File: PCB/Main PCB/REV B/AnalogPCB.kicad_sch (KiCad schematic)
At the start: 77 parts, among them J1 DF12NB_4.0_-20DP-0.5V_51_, J2 393570002, J3 393570002, J4 393570002, J5 393570002, J6 SJ3-35053D, Q1 2N7002, Q2 2N7002, Q3 2N7002, U1 ALDP105W, U2 ALDP105W, U3 ALDP105W

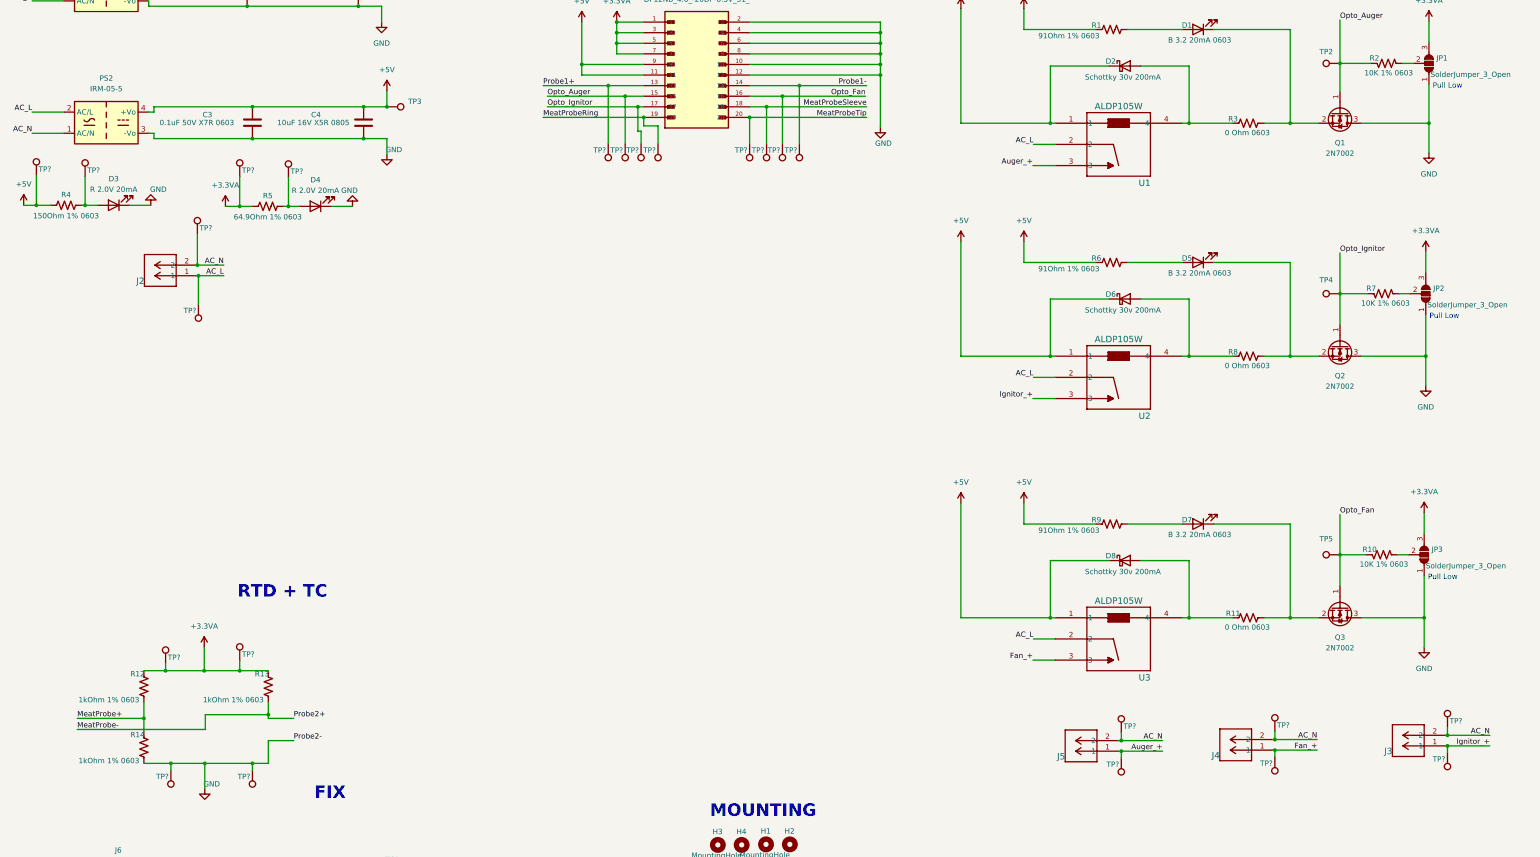
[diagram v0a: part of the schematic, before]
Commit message: PCB - Grouping for digital layout
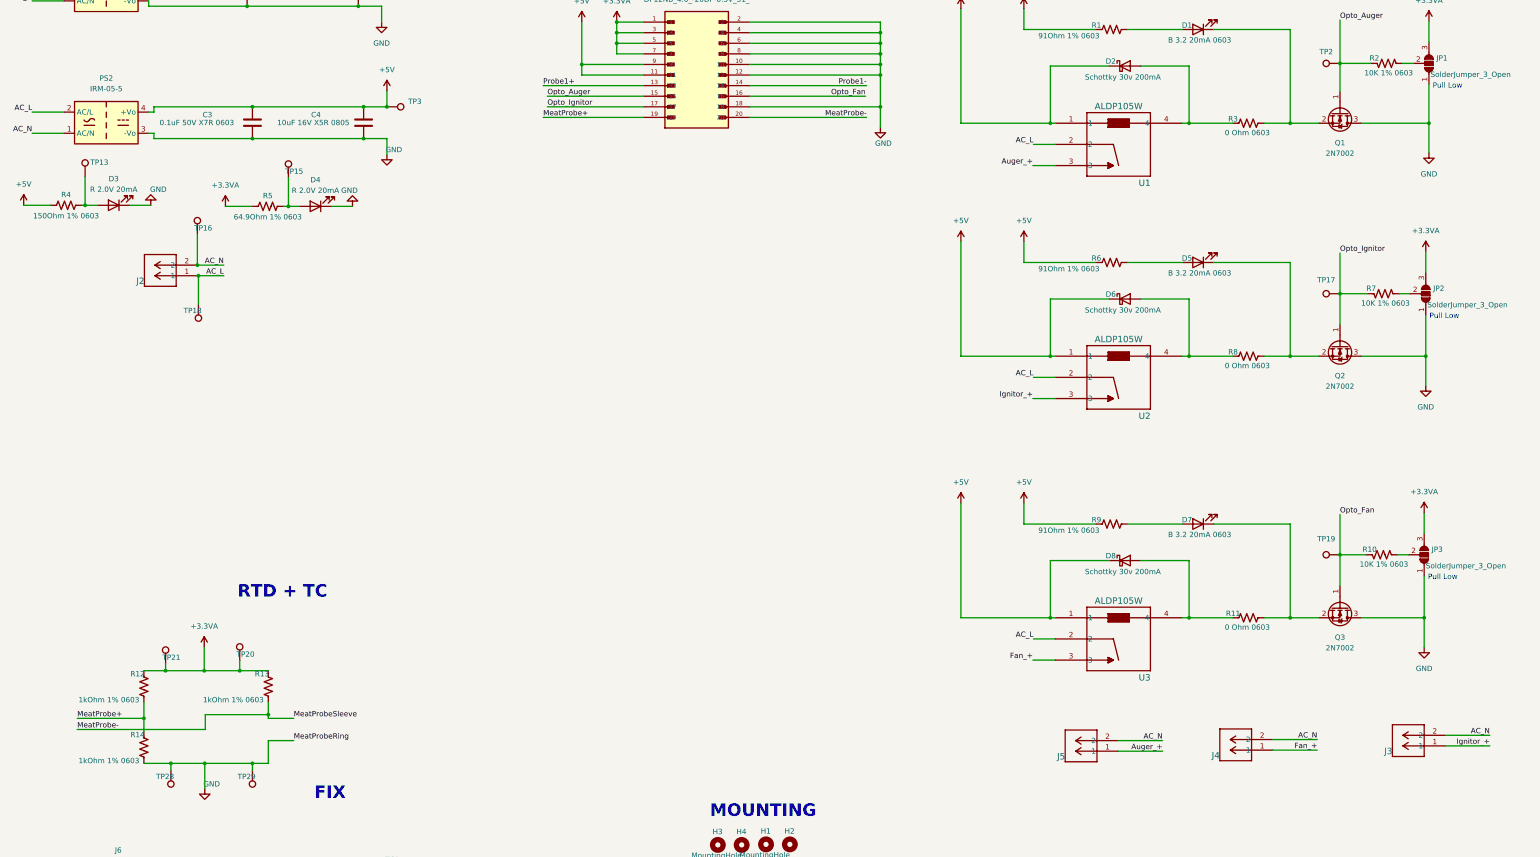
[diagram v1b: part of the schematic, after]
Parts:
- removed TP? (x16): TP, TestPoint:TestPoint_Pad_D1.0mm, symbol Connector:TestPoint
- gave numbers to parts that had none: 8
- renumbered TP4 to TP17, TP5 to TP19
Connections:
- net GND: now also J1.18, J6.3
- net MeatProbe+: now also J1.19
- net MeatProbe-: now also J1.20, J6.1
- net MeatProbeTip: no longer J1.20
- removed net MeatProbeRing: J1.19, J6.3
- removed net MeatProbeSleeve: J1.18, J6.1

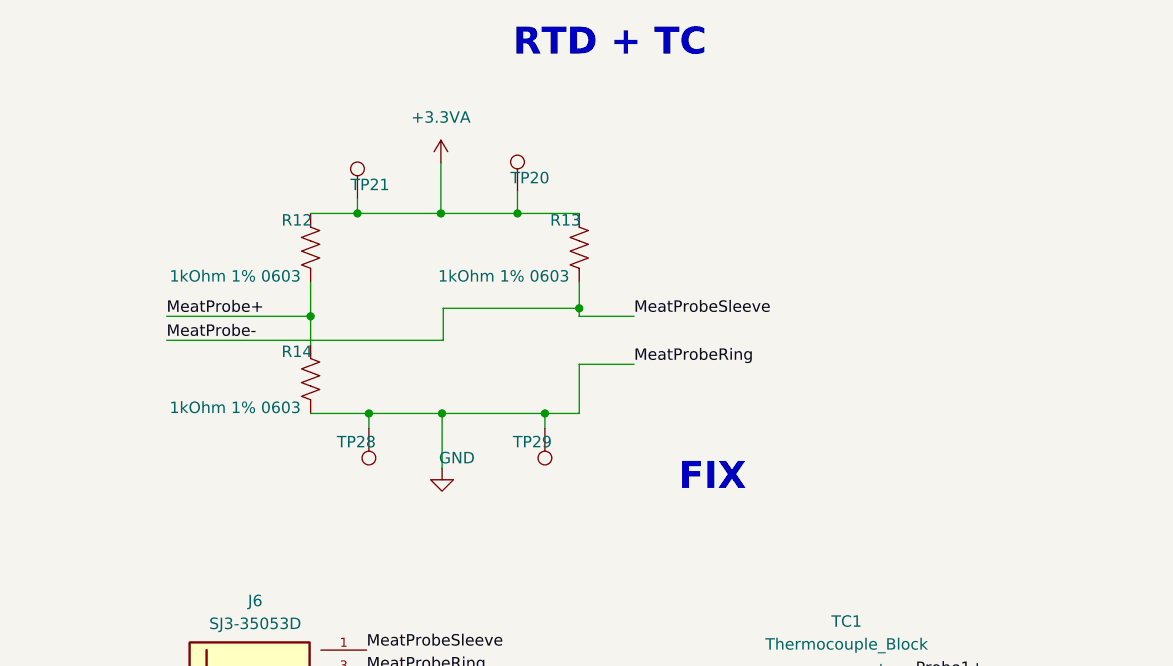
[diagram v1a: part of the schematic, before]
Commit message: PCB - Digital/analog layout complete - ready to review
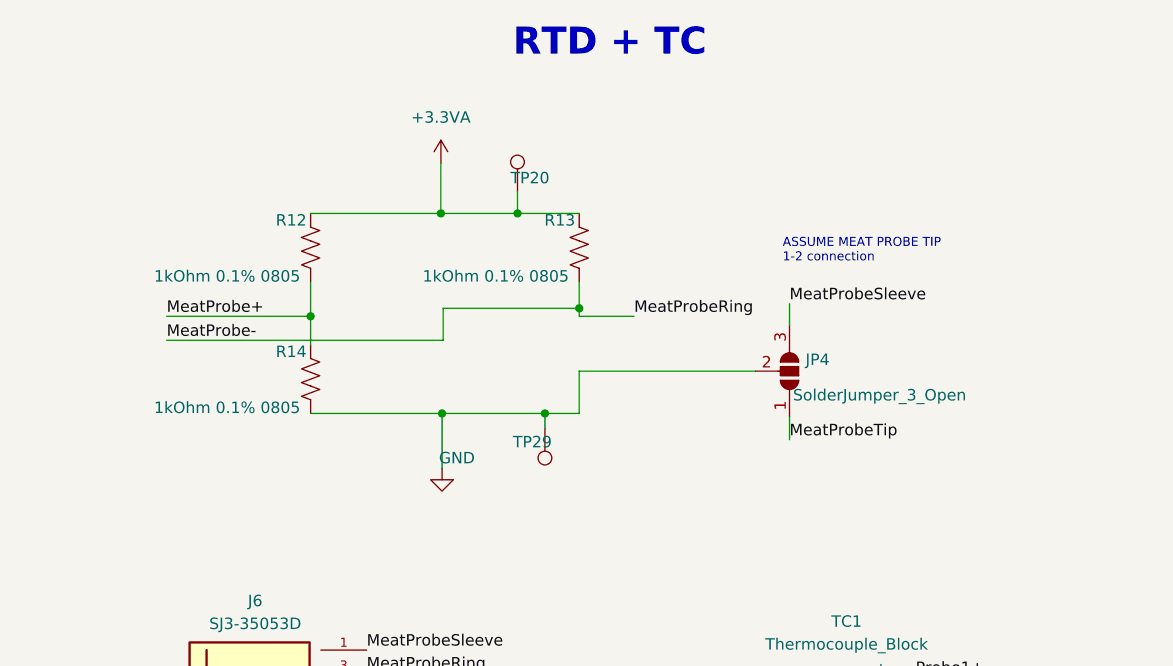
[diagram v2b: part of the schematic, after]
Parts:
- removed TP21, TP28: TP, TestPoint:TestPoint_Pad_D1.0mm, symbol Connector:TestPoint
- added JP4: SolderJumper_3_Open, Jumper:SolderJumper-3_P1.3mm_Open_RoundedPad1.0x1.5mm, symbol Jumper:SolderJumper_3_Open
- R12, R13, R14: value 1kOhm 1% 0603 -> 1kOhm 0.1% 0805; footprint Resistor_SMD:R_0603_1608Metric -> Resistor_SMD:R_0805_2012Metric; Manufacturer YAGEO -> Susumu; Manufacturer Part Number RC0603FR-071KL -> RG2012P-102-B-T5; Vendor Part Number 311-1.00KHRCT-ND -> RG20P1.0KBCT-ND
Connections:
- net GND: now also JP4.2 (C); no longer J6.3
- net MeatProbe-: now also J6.3; no longer J6.1
- net MeatProbeTip: now also JP4.1 (A)
- new net MeatProbeSleeve: J6.1, JP4.3 (B)
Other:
- note added: "ASSUME MEAT PROBE TIP 1-2 connection"
- note removed: "FIX"

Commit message: PCB - Analog pcb under review and making minor mods - diode placement
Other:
- note added: "Needs to have AC power to switch a load"
- moved on the sheet: C1, C2, C3, C4, D3, D4, H1, H2, H3, H4, J1, J2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

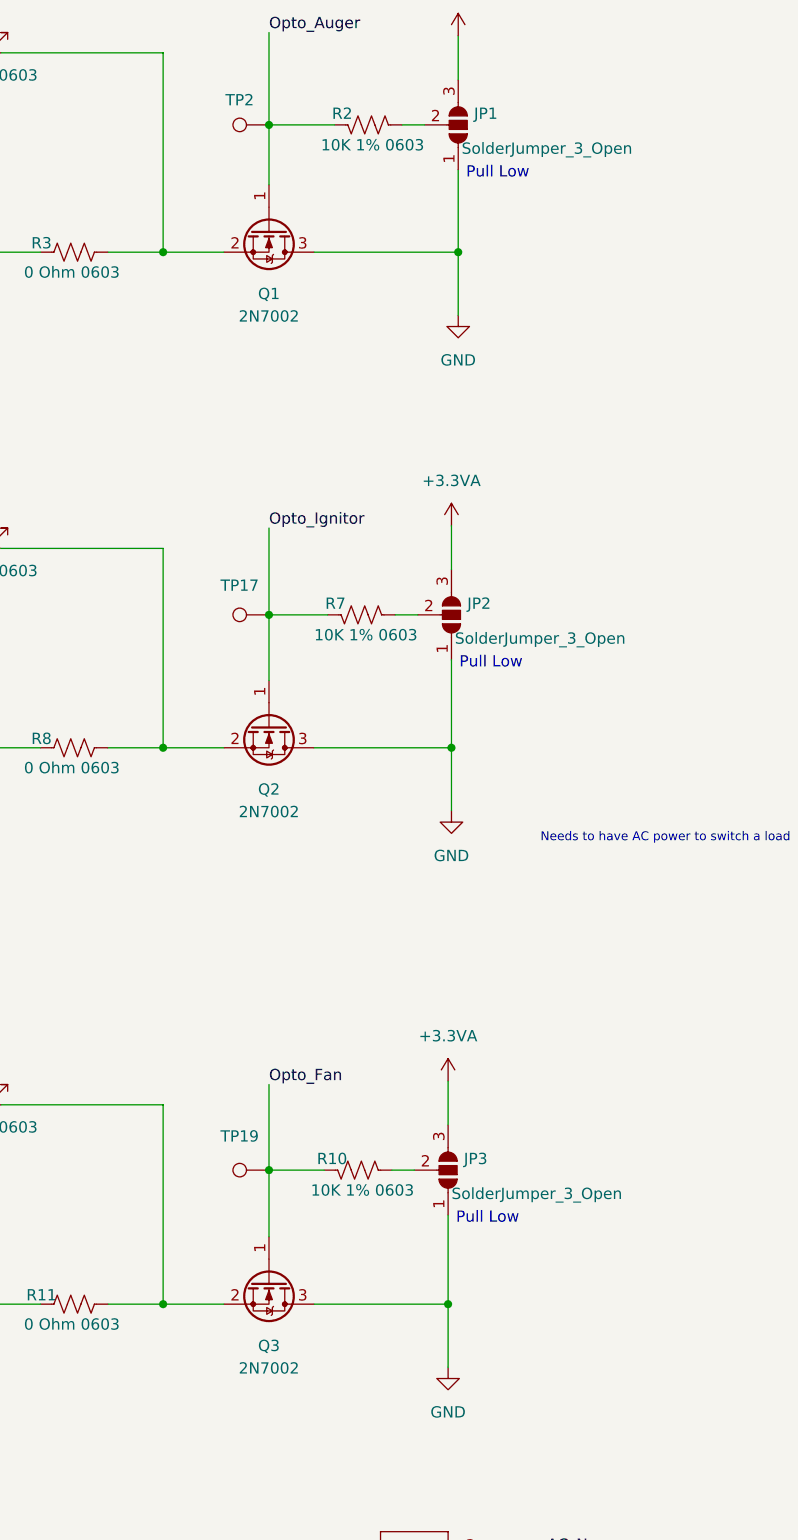
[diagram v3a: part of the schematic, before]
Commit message: PCB - gerbers generated and boms started
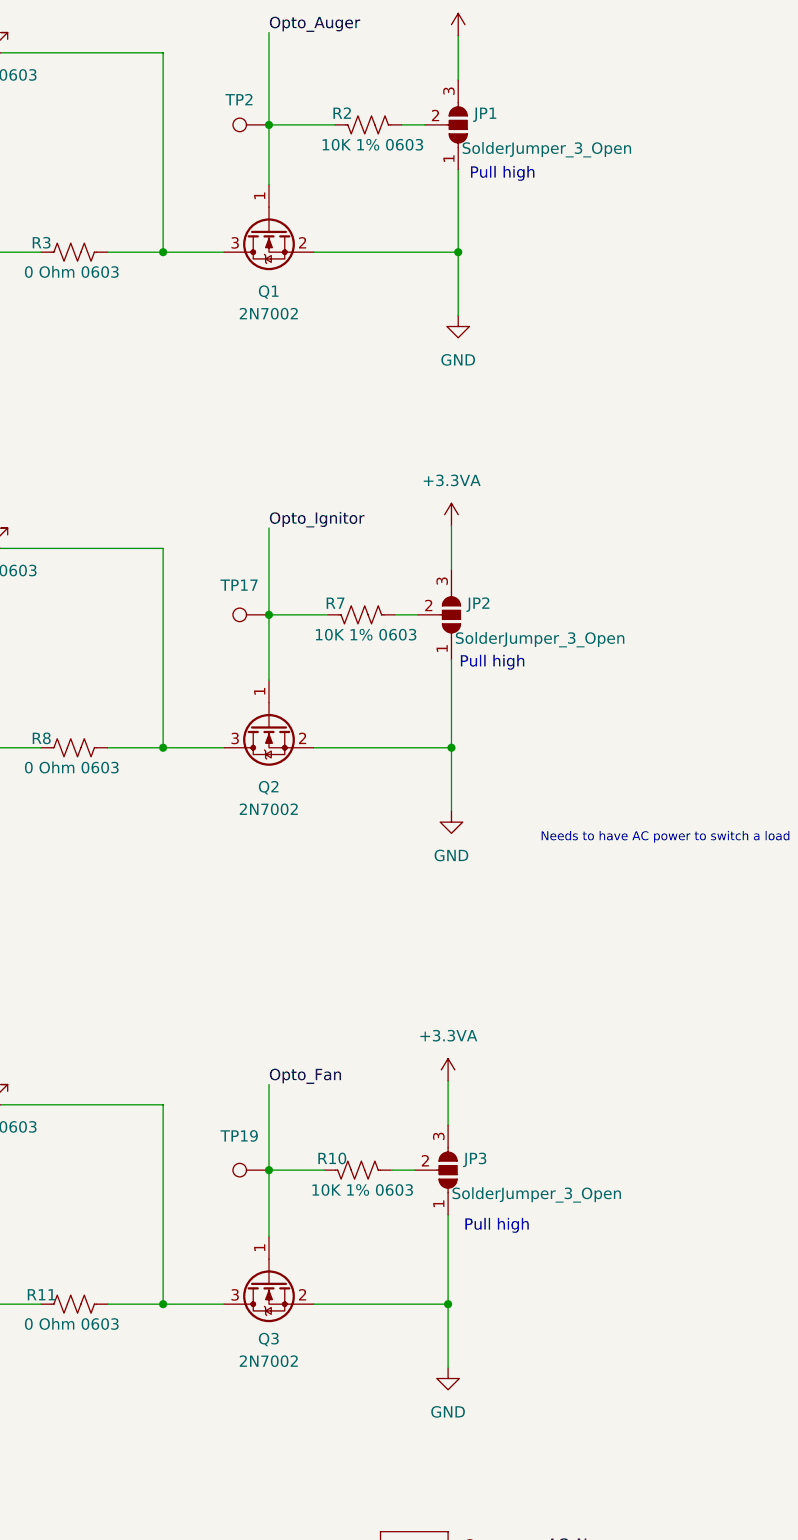
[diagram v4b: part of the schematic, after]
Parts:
- PS2: Manufacturer (none) -> MEAN WELL USA Inc.; Manufacturer Part Number (none) -> IRM-05-5; Vendor (none) -> Digikey; Vendor Part Number (none) -> 1866-3027-ND
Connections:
- net GND: now also Q1.2 (S), Q2.2 (S), Q3.2 (S); no longer Q1.3 (D), Q2.3 (D), Q3.3 (D)
- net at D7.1 (K), R11.2: now also Q3.3 (D); no longer Q3.2 (S)
- net at D1.1 (K), R3.2: now also Q1.3 (D); no longer Q1.2 (S)
- net at D5.1 (K), R8.2: now also Q2.3 (D); no longer Q2.2 (S)
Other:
- note added: "Pull high"
- note removed: "Pull Low"
- moved on the sheet: Q1, Q2, Q3
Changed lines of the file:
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@@
     (effects (font (size 3 3) (thickness 1.016) bold) (justify left bottom))
   )
-  (text "Pull Low" (at 360.426 64.897 0)
-    (effects (font (size 1.27 1.27)) (justify left bottom))
-  )
-  (text "Pull Low" (at 359.664 120.142 0)
+  (text "Pull high" (at 360.172 183.642 0)
+    (effects (font (size 1.27 1.27)) (justify left bottom))
+  )
+  (text "Pull high" (at 359.664 120.142 0)
     (effects (font (size 1.27 1.27)) (justify left bottom))
   )
@@
     (effects (font (size 1 1)) (justify left bottom))
   )
+  (text "Pull high" (at 360.807 65.024 0)
+    (effects (font (size 1.27 1.27)) (justify left bottom))
+  )
   (text "ASSUME MEAT PROBE TIP \n1-2 connection" (at 95.631 213.995 0)
     (effects (font (size 1 1)) (justify left bottom))
@@
   (text "LOADS" (at 311.277 32.639 0)
     (effects (font (size 3 3) (thickness 1.016) bold) (justify left bottom))
-  )
-  (text "Pull Low" (at 359.283 182.753 0)
-    (effects (font (size 1.27 1.27)) (justify left bottom))
   )
   (text "INTERFACE" (at 171.196 88.011 0)
@@
     (pin "1")
   )
-  (symbol (lib_id "Transistor_FET:2N7002") (at 338.201 70.485 270) (unit 1)
-    (in_bom yes) (on_board yes) (fields_autoplaced)
-    (property "Reference" "Q1" (id 0) (at 338.201 77.724 90))
-    (property "Value" "2N7002" (id 1) (at 338.201 80.264 90))
-    (property "Footprint" "Package_TO_SOT_SMD:SOT-23" (id 2) (at 336.296 75.565 0)
+  (symbol (lib_id "Transistor_FET:2N7002") (at 338.201 70.485 90) (mirror x) (unit 1)
+    (in_bom yes) (on_board yes) (fields_autoplaced)
+    (property "Reference" "Q1" (id 0) (at 338.201 77.47 90))
+    (property "Value" "2N7002" (id 1) (at 338.201 80.01 90))
+    (property "Footprint" "Package_TO_SOT_SMD:SOT-23" (id 2) (at 340.106 75.565 0)
       (effects (font (size 1.27 1.27) italic) (justify left) hide)
     )
@@
     (pin "3")
   )
-  (symbol (lib_id "Transistor_FET:2N7002") (at 338.201 189.103 270) (unit 1)
-    (in_bom yes) (on_board yes) (fields_autoplaced)
-    (property "Reference" "Q3" (id 0) (at 338.201 196.342 90))
-    (property "Value" "2N7002" (id 1) (at 338.201 198.882 90))
-    (property "Footprint" "Package_TO_SOT_SMD:SOT-23" (id 2) (at 336.296 194.183 0)
+  (symbol (lib_id "Transistor_FET:2N7002") (at 338.201 189.103 90) (mirror x) (unit 1)
+    (in_bom yes) (on_board yes) (fields_autoplaced)
+    (property "Reference" "Q3" (id 0) (at 338.201 195.58 90))
+    (property "Value" "2N7002" (id 1) (at 338.201 198.12 90))
+    (property "Footprint" "Package_TO_SOT_SMD:SOT-23" (id 2) (at 340.106 194.183 0)
       (effects (font (size 1.27 1.27) italic) (justify left) hide)
     )
@@
       (effects (font (size 1.27 1.27)) hide)
     )
+    (property "Manufacturer" "MEAN WELL USA Inc." (id 4) (at 49.403 113.157 0)
+      (effects (font (size 1.27 1.27)) hide)
+    )
+    (property "Manufacturer Part Number" "IRM-05-5" (id 5) (at 49.403 113.157 0)
+      (effects (font (size 1.27 1.27)) hide)
+    )
+    (property "Vendor" "Digikey" (id 6) (at 49.403 113.157 0)
+      (effects (font (size 1.27 1.27)) hide)
+    )
+    (property "Vendor Part Number" "1866-3027-ND" (id 7) (at 49.403 113.157 0)
+      (effects (font (size 1.27 1.27)) hide)
+    )
     (pin "1")
     (pin "2")
@@
     (pin "2")
   )
-  (symbol (lib_id "Transistor_FET:2N7002") (at 338.201 126.365 270) (unit 1)
-    (in_bom yes) (on_board yes) (fields_autoplaced)
-    (property "Reference" "Q2" (id 0) (at 338.201 133.604 90))
-    (property "Value" "2N7002" (id 1) (at 338.201 136.144 90))
-    (property "Footprint" "Package_TO_SOT_SMD:SOT-23" (id 2) (at 336.296 131.445 0)
+  (symbol (lib_id "Transistor_FET:2N7002") (at 338.201 126.365 90) (mirror x) (unit 1)
+    (in_bom yes) (on_board yes) (fields_autoplaced)
+    (property "Reference" "Q2" (id 0) (at 338.201 133.35 90))
+    (property "Value" "2N7002" (id 1) (at 338.201 135.89 90))
+    (property "Footprint" "Package_TO_SOT_SMD:SOT-23" (id 2) (at 340.106 131.445 0)
       (effects (font (size 1.27 1.27) italic) (justify left) hide)
     )
